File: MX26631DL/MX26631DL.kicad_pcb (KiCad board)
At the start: 4 copper layers, 21 x 22.6 mm, 14 parts, among them U1 ESDBW5V0A1_C5173252, U2 MX26631DL

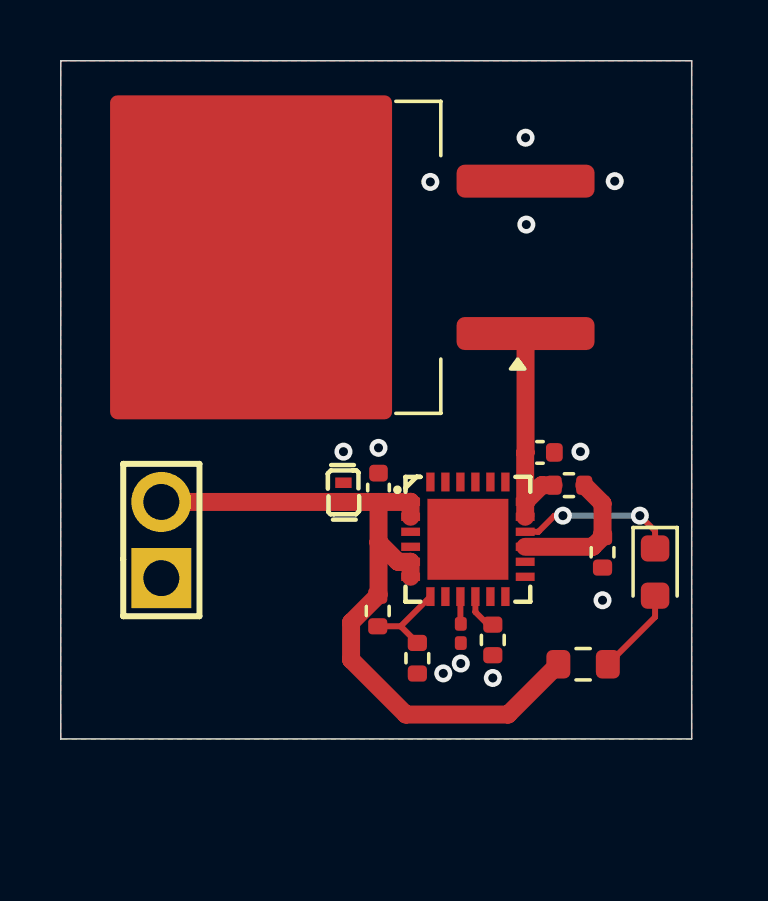
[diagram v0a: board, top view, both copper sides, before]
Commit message: Changed capacitor size
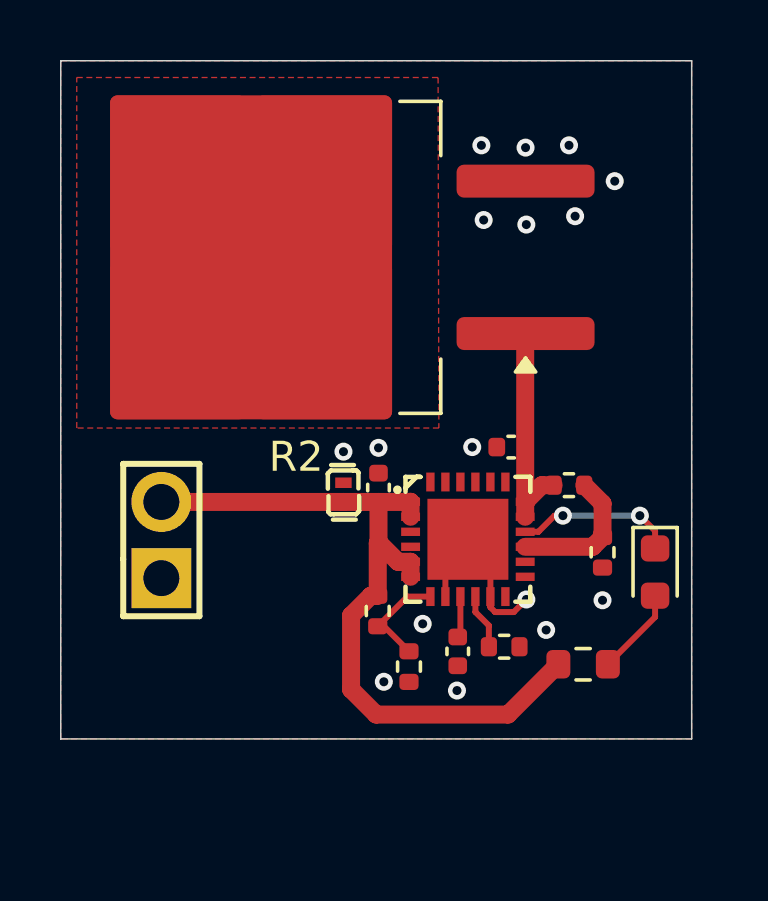
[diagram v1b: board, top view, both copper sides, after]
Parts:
- C16: value 10uF -> 100nF
- C17: footprint Capacitor_SMD:C_0201_0603Metric -> Capacitor_SMD:C_0402_1005Metric
- R2: footprint Package_TO_SOT_SMD:TO-263-2_TabPin1 -> Package_TO_SOT_SMD:TO-263-2
- moved C16 0.98 mm to (109.5, 90.9), turned to 180 degrees
- moved C17 0.61 mm to (107.7, 97.7)
- moved R10 0.44 mm to (109.2, 97.6), turned to 0 degrees
- moved R14 0.40 mm to (106.0, 98.2)
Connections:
- R2 pad 2: GND -> Heatsink
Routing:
- net GND: track 0.00 -> 6.24 mm, vias 11 -> 16
- net /+5V_unprot: track 24.6 -> 25.4 mm
- net Net-(U2-OVP): track 2.95 -> 3.55 mm
- net Net-(U2-ILIM): track 1.27 -> 1.86 mm
- added copper zone on F.Cu, net Heatsink

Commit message: Testboard is done, production files generated
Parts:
- removed C17: 100nF, Capacitor_SMD:C_0402_1005Metric
- removed U1: ESDBW5V0A1_C5173252, easyeda2kicad:X1-DFN1006-2_L1.0-W0.6-P0.65-BI
- added U4: TPESD0402G15V, Diode_SMD:D_0402_1005Metric, F.Cu at (103.9, 92.3)
- C16: value 100nF -> 10uF
- R10: value 11kR -> 6.2kR
- moved R12 1.41 mm to (111.8, 95.6)
- moved R10 0.97 mm to (108.3, 97.5), turned to -90 degrees
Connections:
- U2 pad 9: Net-(U2-dVdT) -> unconnected-(U2-dVdT-Pad9)
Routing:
- net GND: track 6.24 -> 4.44 mm, vias 16 -> 17
- net Net-(U2-dVdT): track 1.38 -> 0.00 mm
- net Net-(U2-PGTH): track 4.69 -> 5.83 mm
- net Net-(U2-ILIM): track 1.86 -> 1.06 mm
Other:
- board text added: "+"
- board text added: "-"
- board text added: "Surge IC Test Board MX26631DL Phakin Dhamsirimongkol"
- board text removed: "Powerline Protection IC MX26631DL Phakin Dhamsirimongkol"

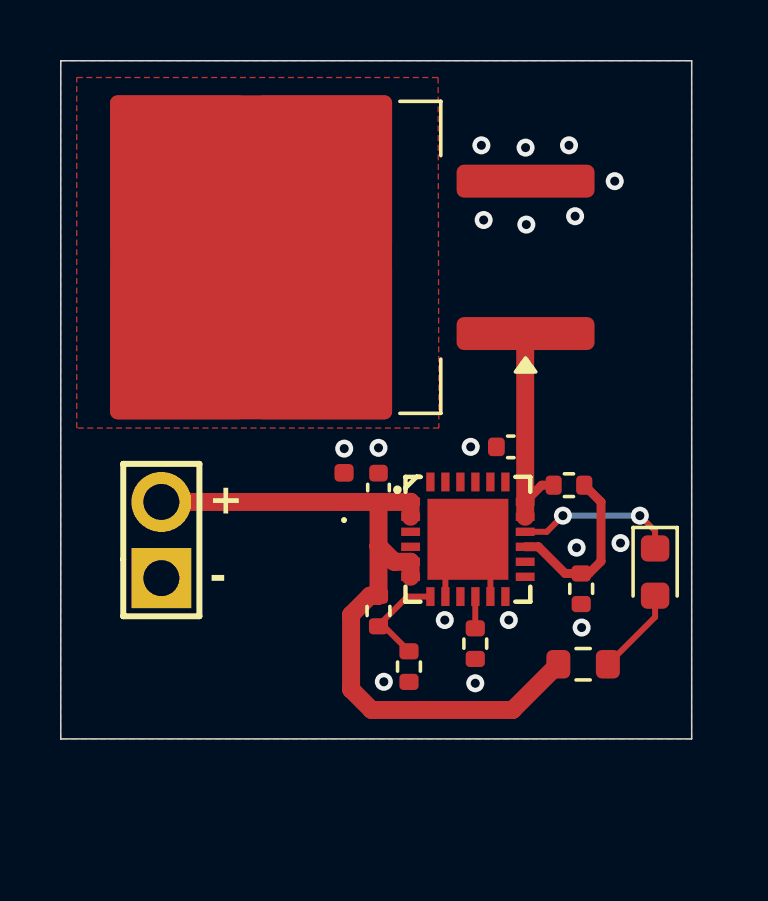
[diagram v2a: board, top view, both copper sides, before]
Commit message: Added dVdT capacitor to reduce current inrush. Production files generated
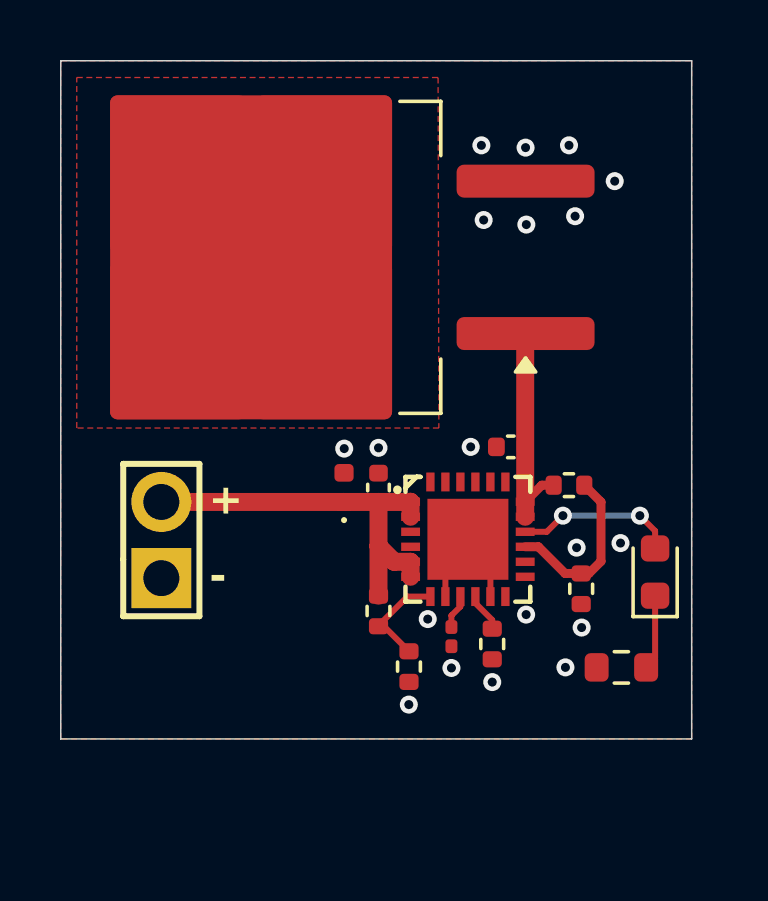
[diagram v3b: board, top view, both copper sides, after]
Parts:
- added C1: 100nF, Capacitor_SMD:C_0201_0603Metric, F.Cu at (107.5, 97.2)
- moved R1 1.28 mm to (113.1, 98.2)
- moved R10 0.57 mm to (108.8, 97.5)
- turned D1 to 90 degrees
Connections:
- D1 pad 1: /PGOOD -> Net-(D1-K)
- D1 pad 2: Net-(D1-A) -> /PGOOD
- R1 pad 1: Net-(D1-A) -> Net-(D1-K)
- R1 pad 2: /+5V_unprot -> GND
- U2 pad 9: unconnected-(U2-dVdT-Pad9) -> Net-(U2-dVdT)
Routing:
- net /+5V_unprot: track 25.2 -> 13.7 mm
- net Net-(D1-A): track 2.94 -> 0.00 mm
- net Net-(D1-K): track 0.00 -> 2.51 mm
- net Net-(U2-dVdT): track 0.00 -> 1.14 mm
- net GND: vias 17 -> 19

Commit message: Need to verify circuit 1 more time
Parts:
- removed C15, C16: 10uF, Capacitor_SMD:C_0402_1005Metric
- removed H1: X6511WV-02H-C30D60, easyeda2kicad:HDR-TH_2P-P2.54-V-M
- removed R10: 6.2kR, Resistor_SMD:R_0402_1005Metric
- removed R11: 27kR, Resistor_SMD:R_0402_1005Metric
- removed R12, R14: 10kR, Resistor_SMD:R_0402_1005Metric
- removed R13: 39kR, Resistor_SMD:R_0402_1005Metric
- added C2: 100nF, Capacitor_SMD:C_0402_1005Metric_Pad0.74x0.62mm_HandSolder, F.Cu at (107.1, 98.3)
- added C3: 10uF, Capacitor_SMD:C_0805_2012Metric_Pad1.18x1.45mm_HandSolder, F.Cu at (112.3, 91.5)
- added R3: 20kR, Resistor_SMD:R_0603_1608Metric_Pad0.98x0.95mm_HandSolder, F.Cu at (110.6, 98.2)
- added R4: 2kR, Resistor_SMD:R_0603_1608Metric, F.Cu at (100.8, 99.2)
- added R5: 31.6kR, Resistor_SMD:R_0603_1608Metric, F.Cu at (111.4, 94.2)
- added R6: 10kR, Resistor_SMD:R_0402_1005Metric_Pad0.72x0.64mm_HandSolder, F.Cu at (112.2, 96.3)
- added R7: 10R, Resistor_SMD:R_0603_1608Metric_Pad0.98x0.95mm_HandSolder, F.Cu at (111.4, 87.2)
- added U1: ZX-PZ2.54-1-1PZZ, easyeda2kicad:HDR-TH_1P-P2.54-V-M, F.Cu at (97.9, 88.1)
- added U3: TPESD0402G15V, Diode_SMD:D_0402_1005Metric, F.Cu at (102.5, 92.5)
- C1: value 100nF -> 10uF; footprint Capacitor_SMD:C_0201_0603Metric -> Capacitor_SMD:C_0805_2012Metric_Pad1.18x1.45mm_HandSolder
- R1: value 2kR -> 39kR; footprint Resistor_SMD:R_0603_1608Metric -> Resistor_SMD:R_0402_1005Metric_Pad0.72x0.64mm_HandSolder
- R2: value 2R -> 10kR; footprint Package_TO_SOT_SMD:TO-263-2 -> Resistor_SMD:R_0402_1005Metric_Pad0.72x0.64mm_HandSolder
- U2: value MX26631DL -> ZX-PZ2.54-1-1PZZ; footprint easyeda2kicad:QFN-24_L4.0-W4.0-P0.50-TL-EP2.7 -> easyeda2kicad:HDR-TH_1P-P2.54-V-M
- U4: value TPESD0402G15V -> MX26631DL; footprint Diode_SMD:D_0402_1005Metric -> easyeda2kicad:QFN-24_L4.0-W4.0-P0.50-TL-EP2.7
- moved R2 14.8 mm to (105.9, 98.9), turned to -90 degrees
- moved D1 12.3 mm to (103.3, 100.7), turned to 180 degrees
- moved U2 11.4 mm to (97.9, 99.2)
- moved R1 8.57 mm to (104.6, 97.0), turned to 0 degrees
- moved C1 6.24 mm to (104.0, 92.0), turned to 90 degrees
- moved U4 3.96 mm to (107.3, 94.2), turned to 0 degrees
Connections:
- C1 pad 1: Net-(U2-dVdT) -> /+5V_unprot
- D1 pad 1: Net-(D1-K) -> /PGOOD
- D1 pad 2: /PGOOD -> Net-(D1-A)
- R1 pad 1: Net-(D1-K) -> /+5V_unprot
- R1 pad 2: GND -> Net-(U4-OVP)
- R2 pad 1: Net-(C16-Pad1) -> Net-(U4-OVP)
- R2 pad 2: Heatsink -> GND
- U2 pad 1: /+5V_unprot -> GND
- U4 pad 2: GND -> /+5V_unprot
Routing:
- net /PGOOD: track 5.35 -> 21.4 mm, vias 2 -> 0
- net GND: track 4.44 -> 15.6 mm, vias 19 -> 10
- net Net-(C3-Pad1): track 0.00 -> 7.66 mm
- net Net-(C16-Pad1): track 7.29 -> 0.00 mm
- net /+5V_unprot: track 13.7 -> 20.7 mm
- net Net-(U2-PGTH): track 5.83 -> 0.00 mm
- net Net-(U4-PGTH): track 0.00 -> 3.86 mm
- net Net-(U2-OVP): track 3.55 -> 0.00 mm
- net Net-(U4-ILIM): track 0.00 -> 3.47 mm
- net Net-(U4-OVP): track 0.00 -> 2.99 mm
- net Net-(D1-K): track 2.51 -> 0.00 mm
- net Net-(D1-A): track 0.00 -> 1.91 mm
- net Net-(U4-dVdT): track 0.00 -> 1.65 mm
- net Net-(U2-ILIM): track 1.31 -> 0.00 mm
- net Net-(U2-dVdT): track 1.14 -> 0.00 mm
- added copper zone on B.Cu, net GND
- removed copper zone on F.Cu, net GND
- removed copper zone on In1.Cu, net GND
- removed copper zone on In2.Cu, net GND
- removed copper zone on F.Cu, net Heatsink
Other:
- board size 21 x 22.6 mm -> 21 x 21 mm
- copper layers 4 -> 2
- board text added: "Output Resistor 500mA"
- board text removed: "+"
- board text removed: "-"

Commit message: Time to test
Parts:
- R1: value 39kR -> 37.4kR
- R5: value 31.6kR -> 29.4kR
- R7: footprint Resistor_SMD:R_0603_1608Metric_Pad0.98x0.95mm_HandSolder -> Resistor_SMD:R_2512_6332Metric_Pad1.40x3.35mm_HandSolder
- moved R7 4.58 mm to (106.9, 86.1), turned to 180 degrees
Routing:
- net Net-(C3-Pad1): track 7.66 -> 10.2 mm
- net GND: track 15.6 -> 16.7 mm
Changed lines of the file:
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@@
 			)
 		)
-		(property "Value" "31.6kR"
+		(property "Value" "29.4kR"
 			(at 0 1.43 90)
 			(layer "F.Fab")
@@
 			)
 		)
-		(property "LCSC Part" "C2933196"
+		(property "LCSC Part" "C2930086"
 			(at 0 0 270)
 			(unlocked yes)
@@
 			)
 		)
-		(property "Value" "39kR"
+		(property "Value" "37.4kR"
 			(at 0 1.17 0)
 			(layer "F.Fab")
@@
 			)
 		)
-		(property "LCSC Part" "C2930006"
+		(property "LCSC Part" "C185422"
 			(at 0 0 0)
 			(unlocked yes)
@@
 		)
 	)
-	(footprint "Resistor_SMD:R_0603_1608Metric_Pad0.98x0.95mm_HandSolder"
+	(footprint "Resistor_SMD:R_2512_6332Metric_Pad1.40x3.35mm_HandSolder"
 		(layer "F.Cu")
-		(at 111.375 87.215 90)
-		(descr "Resistor SMD 0603 (1608 Metric), square (rectangular) end terminal, IPC_7351 nominal with elongated pad for handsoldering. (Body size source: IPC-SM-782 page 72, https://www.pcb-3d.com/wordpress/wp-content/uploads/ipc-sm-782a_amendment_1_and_2.pdf), generated with kicad-footprint-generator")
+		(at 106.925 86.125 180)
+		(descr "Resistor SMD 2512 (6332 Metric), square (rectangular) end terminal, IPC_7351 nominal with elongated pad for handsoldering. (Body size source: IPC-SM-782 page 72, https://www.pcb-3d.com/wordpress/wp-content/uploads/ipc-sm-782a_amendment_1_and_2.pdf), generated with kicad-footprint-generator")
 		(tags "resistor handsolder")
 		(property "Reference" "R7"
-			(at 0 -1.43 90)
+			(at 0 -2.62 0)
 			(layer "F.SilkS")
 			(effects
@@
 		)
 		(property "Value" "10R"
-			(at 0 1.43 90)
+			(at 0 2.62 0)
 			(layer "F.Fab")
 			(effects
@@
 		)
 		(property "Datasheet" ""
-			(at 0 0 90)
+			(at 0 0 180)
 			(unlocked yes)
 			(layer "F.Fab")
@@
 		)
 		(property "Description" "Resistor"
-			(at 0 0 90)
+			(at 0 0 180)
 			(unlocked yes)
 			(layer "F.Fab")
@@
 			)
 		)
-		(property "LCSC Part" "C109318"
-			(at 0 0 90)
+		(property "LCSC Part" "C2075790"
+			(at 0 0 180)
 			(unlocked yes)
 			(layer "F.Fab")
@@
 		(attr smd)
 		(fp_line
-			(start -0.254724 -0.5225)
-			(end 0.254724 -0.5225)
+			(start -2.177064 1.71)
+			(end 2.177064 1.71)
 			(stroke
 				(width 0.12)
@@
 		)
 		(fp_line
-			(start -0.254724 0.5225)
-			(end 0.254724 0.5225)
+			(start -2.177064 -1.71)
+			(end 2.177064 -1.71)
 			(stroke
 				(width 0.12)
@@
 		)
 		(fp_line
-			(start 1.65 -0.73)
-			(end 1.65 0.73)
+			(start 4 1.92)
+			(end -4 1.92)
 			(stroke
 				(width 0.05)
@@
 		)
 		(fp_line
-			(start -1.65 -0.73)
-			(end 1.65 -0.73)
+			(start 4 -1.92)
+			(end 4 1.92)
 			(stroke
 				(width 0.05)
@@
 		)
 		(fp_line
-			(start 1.65 0.73)
-			(end -1.65 0.73)
+			(start -4 1.92)
+			(end -4 -1.92)
 			(stroke
 				(width 0.05)
@@
 		)
 		(fp_line
-			(start -1.65 0.73)
-			(end -1.65 -0.73)
+			(start -4 -1.92)
+			(end 4 -1.92)
 			(stroke
 				(width 0.05)
@@
 		)
 		(fp_line
-			(start 0.8 -0.4125)
-			(end 0.8 0.4125)
+			(start 3.15 1.6)
+			(end -3.15 1.6)
 			(stroke
 				(width 0.1)
@@
 		)
 		(fp_line
-			(start -0.8 -0.4125)
-			(end 0.8 -0.4125)
+			(start 3.15 -1.6)
+			(end 3.15 1.6)
 			(stroke
 				(width 0.1)
@@
 		)
 		(fp_line
-			(start 0.8 0.4125)
-			(end -0.8 0.4125)
+			(start -3.15 1.6)
+			(end -3.15 -1.6)
 			(stroke
 				(width 0.1)
@@
 		)
 		(fp_line
-			(start -0.8 0.4125)
-			(end -0.8 -0.4125)
+			(start -3.15 -1.6)
+			(end 3.15 -1.6)
 			(stroke
 				(width 0.1)
@@
 		)
 		(fp_text user "${REFERENCE}"
-			(at 0 0 90)
+			(at 0 0 0)
 			(layer "F.Fab")
 			(effects
 				(font
-					(size 0.4 0.4)
-					(thickness 0.06)
+					(size 1 1)
+					(thickness 0.15)
 				)
 			)
 		)
 		(pad "1" smd roundrect
-			(at -0.9125 0 90)
-			(size 0.975 0.95)
+			(at -3.05 0 180)
+			(size 1.4 3.35)
 			(layers "F.Cu" "F.Mask" "F.Paste")
-			(roundrect_rratio 0.25)
+			(roundrect_rratio 0.178571)
 			(net 18 "Net-(C3-Pad1)")
 			(pintype "passive")
 		)
 		(pad "2" smd roundrect
-			(at 0.9125 0 90)
-			(size 0.975 0.95)
+			(at 3.05 0 180)
+			(size 1.4 3.35)
 			(layers "F.Cu" "F.Mask" "F.Paste")
-			(roundrect_rratio 0.25)
+			(roundrect_rratio 0.178571)
 			(net 2 "GND")
 			(pintype "passive")
 		)
 		(embedded_fonts no)
-		(model "${KICAD9_3DMODEL_DIR}/Resistor_SMD.3dshapes/R_0603_1608Metric.wrl"
+		(model "${KICAD9_3DMODEL_DIR}/Resistor_SMD.3dshapes/R_2512_6332Metric.wrl"
 			(offset
 				(xyz 0 0 0)
@@
 	)
 	(gr_text "Output\nResistor\n500mA"
-		(at 114.375 88.175 90)
+		(at 114.808 88.265 90)
 		(layer "F.SilkS")
 		(effects
 			(font
-				(size 0.5 0.5)
-				(thickness 0.1)
+				(size 0.8 0.8)
+				(thickness 0.2)
+				(bold yes)
 			)
 			(justify left bottom)
@@
 	)
 	(segment
-		(start 109.15 96.95)
-		(end 108.5 96.95)
-		(width 0.3)
-		(layer "F.Cu")
-		(net 2)
-	)
-	(segment
 		(start 107.31 94.23)
 		(end 106.56 94.98)
@@
 	)
 	(segment
-		(start 108.5 96.95)
-		(end 108.06 96.51)
+		(start 109.15 96.95)
+		(end 108.250697 96.95)
 		(width 0.3)
 		(layer "F.Cu")
@@
 	)
 	(segment
-		(start 106.56 94.98)
-		(end 106.56 96.14)
+		(start 106.172 97.282)
+		(end 106.56 96.894)
 		(width 0.3)
 		(layer "F.Cu")
@@
 	)
 	(segment
-		(start 106.56 96.615)
+		(start 106.56 94.98)
 		(end 106.56 96.14)
 		(width 0.3)
@@
 	)
 	(segment
-		(start 106.225 96.95)
-		(end 106.56 96.615)
+		(start 108.250697 96.95)
+		(end 108.06 96.759303)
 		(width 0.3)
 		(layer "F.Cu")
@@
 	)
 	(segment
-		(start 111.375 85.175)
-		(end 111.375 86.3025)
-		(width 0.4)
+		(start 106.56 96.894)
+		(end 106.56 96.14)
+		(width 0.3)
 		(layer "F.Cu")
 		(net 2)
@@
 	)
 	(segment
+		(start 103.875 86.125)
+		(end 102.15 86.125)
+		(width 0.3)
+		(layer "F.Cu")
+		(net 2)
+	)
+	(segment
 		(start 113.275 91.45)
 		(end 114.425 91.45)
@@
 	)
 	(segment
-		(start 108.06 96.51)
+		(start 108.06 96.759303)
 		(end 108.06 96.14)
 		(width 0.3)
@@
 	)
 	(via
-		(at 106.225 96.95)
+		(at 106.172 97.282)
 		(size 0.6)
 		(drill 0.3)
@@
 	)
 	(via
-		(at 111.375 85.175)
+		(at 102.15 86.125)
 		(size 0.6)
 		(drill 0.3)
@@
 	)
 	(segment
-		(start 105.156 97.028)
-		(end 105.918 97.79)
+		(start 105.156 97.536)
+		(end 105.918 98.298)
 		(width 0.4)
 		(layer "F.Cu")
@@
 	(segment
 		(start 105.156 96.708001)
-		(end 105.724001 96.14)
+		(end 105.156 97.536)
 		(width 0.4)
 		(layer "F.Cu")
@@
 	)
 	(segment
-		(start 105.156 97.028)
+		(start 105.724001 96.14)
 		(end 105.156 96.708001)
 		(width 0.4)
@@
 	)
 	(segment
-		(start 105.918 97.79)
-		(end 105.918 98.298)
-		(width 0.4)
-		(layer "F.Cu")
-		(net 5)
-	)
-	(segment
-		(start 105.724001 96.14)
-		(end 106.009 96.14)
+		(start 106.009 96.14)
+		(end 105.724001 96.14)
 		(width 0.4)
 		(layer "F.Cu")
@@
 	(segment
 		(start 111.375 93.325)
-		(end 111.375 88.1275)
+		(end 111.375 87.525)
 		(width 0.5)
 		(layer "F.Cu")
@@
 		(width 0.5)
 		(layer "F.Cu")
+		(net 18)
+	)
+	(segment
+		(start 111.375 87.525)
+		(end 109.975 86.125)
+		(width 0.5)
+		(layer "F.Cu")
